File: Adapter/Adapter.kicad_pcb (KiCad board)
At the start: 2 copper layers, 20 x 26 mm, 11 parts, among them J2 Conn_01x14_Socket, U1 BGA153 UFS Modified

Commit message: V1.1
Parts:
- removed J2: Conn_01x14_Socket, BGA153:FPC 14 Pin 0.5P
- added J3: Conn_01x14_Socket, BGA153:FPC 14 Pin 0.5P, F.Cu at (150.0, 102.5)
- U1: footprint BGA153:BGA 153 Modified -> BGA153:BGA 153 Adapter Modified
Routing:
- net /RX0P: track 15.5 -> 8.65 mm, vias 2 -> 0
- net /RX1P: track 15.5 -> 8.65 mm, vias 2 -> 0
- net /RX1N: track 15.4 -> 8.61 mm, vias 2 -> 0
- net /RX0N: track 15.4 -> 8.61 mm, vias 2 -> 0
- net /TX0N: track 15.4 -> 8.65 mm, vias 2 -> 0
- net /TX0P: track 15.4 -> 8.61 mm, vias 2 -> 0
- net /TX1P: track 15.4 -> 8.61 mm, vias 2 -> 0
- net /TX1N: track 15.4 -> 8.65 mm, vias 2 -> 0
- net /RST_N: track 15.4 -> 8.69 mm, vias 2 -> 0
- net VCCQ: track 30.2 -> 23.8 mm
- net VCCQ2: track 29.9 -> 23.7 mm
- net /REF_CLK: track 14.8 -> 8.66 mm, vias 2 -> 0
- net VCC: track 33.7 -> 27.8 mm, vias 3 -> 2
- added copper zone on In1.Cu, net VSS
- added copper zone on In2.Cu, net VSS
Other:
- board size 20 x 26 mm -> 20 x 25 mm
- copper layers 2 -> 4

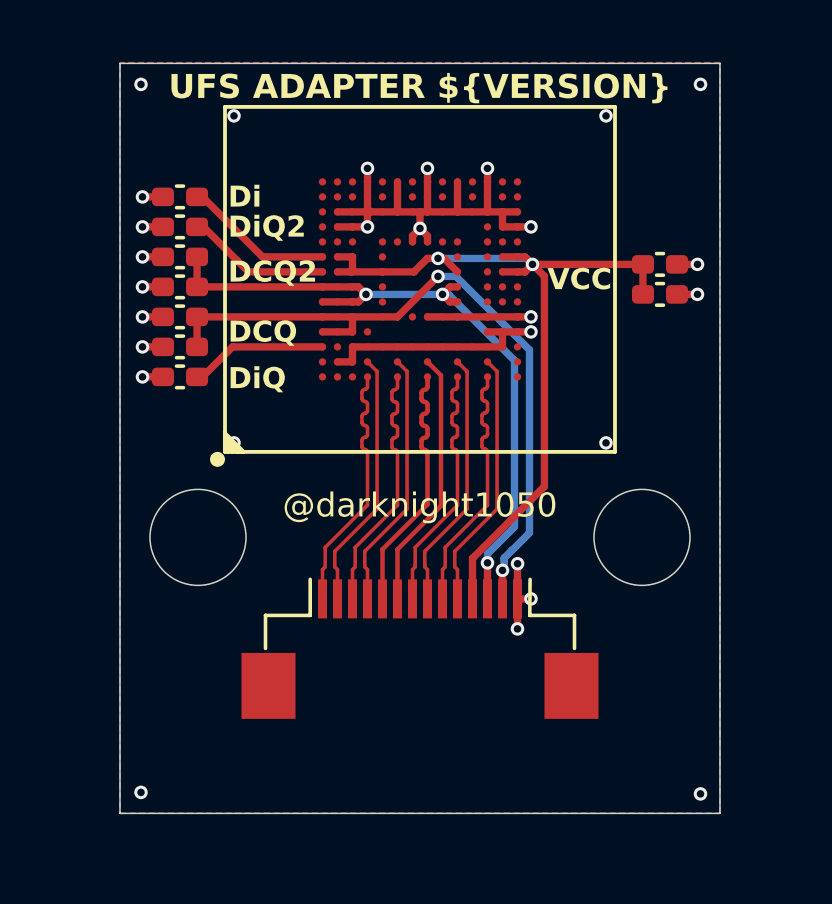
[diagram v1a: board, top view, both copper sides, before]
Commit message: V1.2 for forward fpc cable
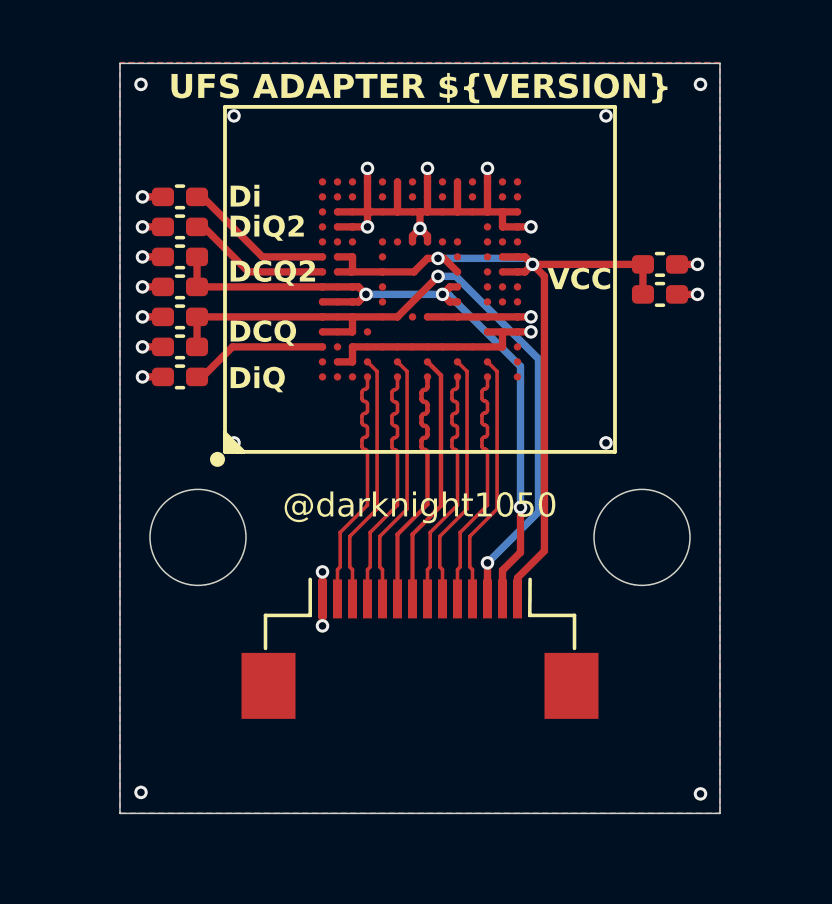
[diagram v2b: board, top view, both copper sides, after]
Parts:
- removed J3: Conn_01x14_Socket, BGA153:FPC 14 Pin 0.5P
- added J2: Conn_01x14_Socket, BGA153:FPC 14 Pin 0.5P, F.Cu at (150.0, 102.5)
- U1: value BGA153 UFS Modified -> BGA153 UFS Adapter Modified
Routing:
- net VSS: track 37.2 -> 36.3 mm, vias 28 -> 27
- net VCC: track 27.8 -> 27.2 mm

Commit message: V1.3 GB042 Connector
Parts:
- removed J2: Conn_01x14_Socket, BGA153:FPC 14 Pin 0.5P
- added J1: GB042-30P-H10, BGA153:GB042-30P-H10, B.Cu at (150.0, 90.0)
- C1, C2, C3, C4, C5, C6, C7, C8, C9: moved to B.Cu
- moved C4 11.9 mm to (152.4, 85.4), turned to 0 degrees
- moved C3 11.6 mm to (152.4, 87.0), turned to 0 degrees
- moved C6 9.41 mm to (150.1, 85.4)
- moved C5 8.35 mm to (150.1, 87.0)
- moved C9 3.58 mm to (144.9, 90.3), turned to -90 degrees
- moved C7 3.20 mm to (145.2, 87.1)
- moved C8 3.20 mm to (145.2, 93.2)
- moved C2 3.15 mm to (155.2, 88.2), turned to 90 degrees
- moved C1 2.85 mm to (155.2, 90.5), turned to -90 degrees
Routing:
- net VCC: track 27.2 -> 14.0 mm
- net VCCQ: track 24.3 -> 11.4 mm, vias 2 -> 1
- net VCCQ2: track 23.6 -> 11.6 mm, vias 3 -> 2
- net /RST_N: track 8.48 -> 19.3 mm, vias 0 -> 1
- net /VDDiQ: track 4.60 -> 10.7 mm, vias 0 -> 2
- net /RX1P: track 8.45 -> 2.84 mm, vias 0 -> 1
- net /RX1N: track 8.40 -> 2.85 mm, vias 0 -> 1
- net /RX0P: track 8.45 -> 2.92 mm, vias 0 -> 1
- net /TX0N: track 8.45 -> 2.92 mm, vias 0 -> 1
- net /RX0N: track 8.40 -> 2.94 mm, vias 0 -> 1
- net /TX0P: track 8.40 -> 2.94 mm, vias 0 -> 1
- net /TX1N: track 8.45 -> 3.00 mm, vias 0 -> 1
- net /TX1P: track 8.40 -> 3.02 mm, vias 0 -> 1
- net /REF_CLK: track 8.45 -> 3.15 mm, vias 0 -> 1
- net VSS: track 36.3 -> 38.3 mm, vias 27 -> 23
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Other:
- board size 20 x 25 mm -> 13 x 11.5 mm
